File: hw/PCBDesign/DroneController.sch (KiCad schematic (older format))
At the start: 5 parts, among them J1 SerialDebug

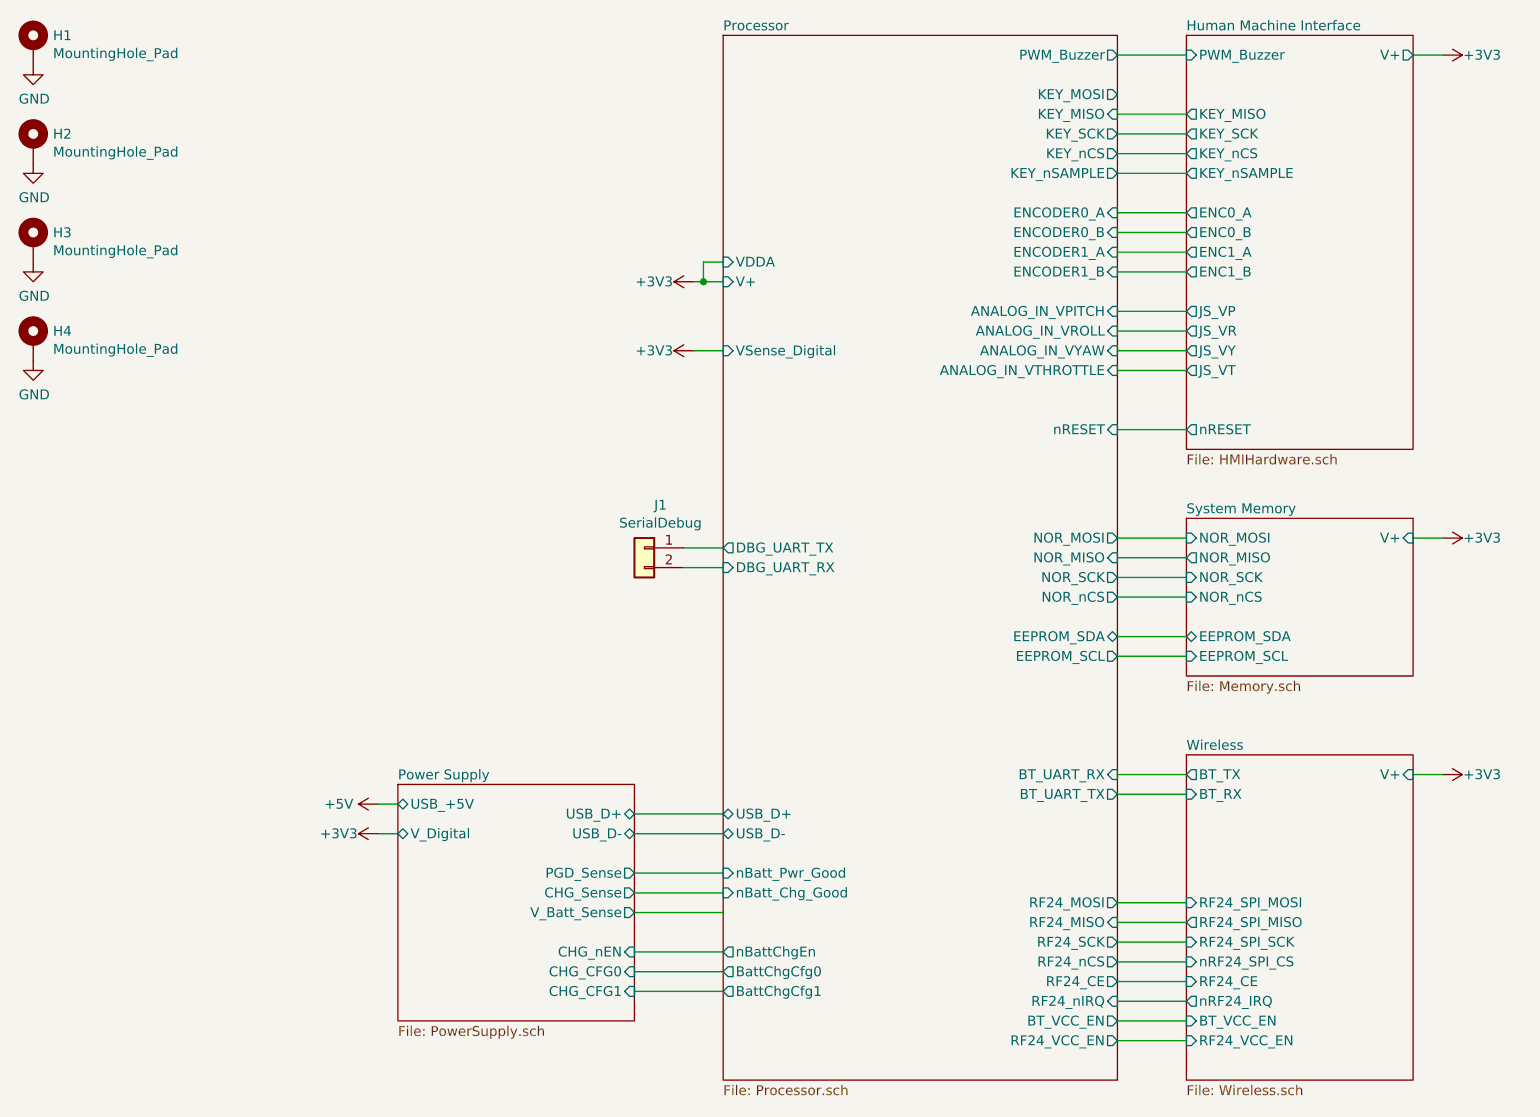
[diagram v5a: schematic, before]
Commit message: Routed most of the core peripherals
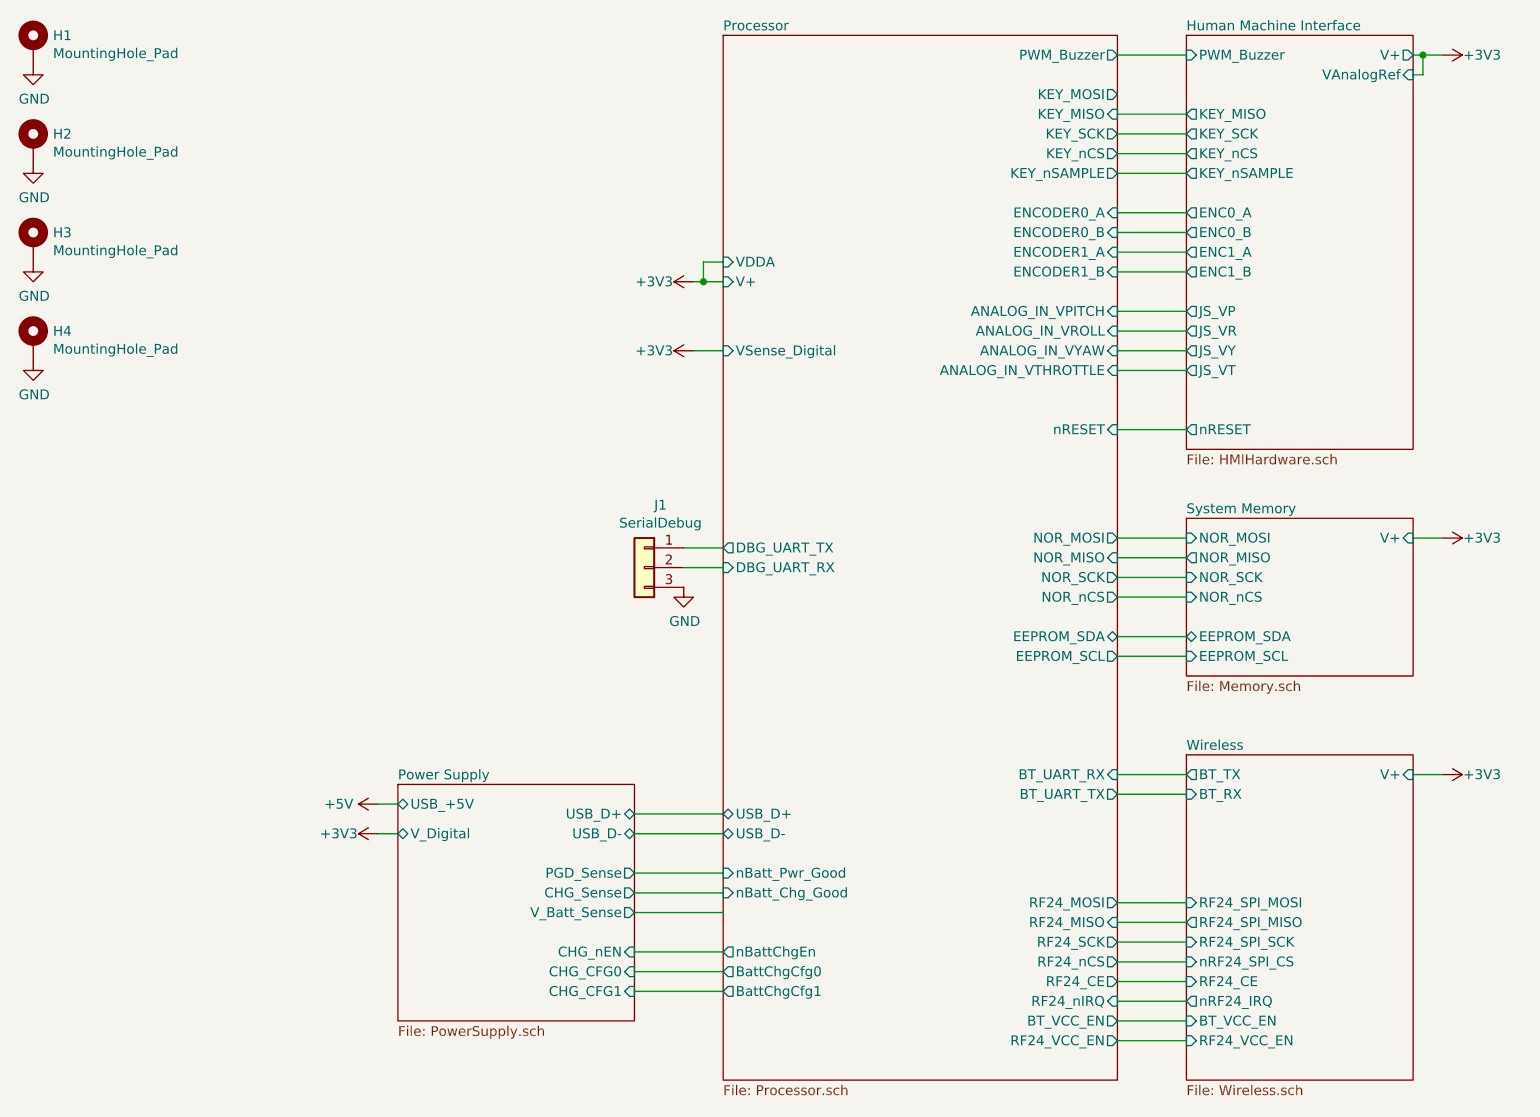
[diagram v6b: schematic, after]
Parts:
- removed J1: SerialDebug, Connector_PinHeader_2.54mm:PinHeader_1x02_P2.54mm_Vertical, symbol Connector_Generic:Conn_01x02
- added J1: SerialDebug, Connector_PinHeader_2.54mm:PinHeader_1x03_P2.54mm_Vertical, symbol Connector_Generic:Conn_01x03
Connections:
- net GND: now also J1.3 (Pin_3)
- net Processor/DBG_UART_RX: now also J1.2 (Pin_2)
- net Processor/DBG_UART_TX: now also J1.1 (Pin_1)
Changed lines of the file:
@@
 F15 "V+" O R 8000 1100 50
 F16 "nRESET" O L 6850 3000 50
+F17 "VAnalogRef" I R 8000 1200 50
 $EndSheet
 $Sheet
@@
 F0 "Wireless" 50
 F1 "Wireless.sch" 50
-F5 "BT_RX" I L 6850 4850 50
-F6 "BT_TX" O L 6850 4750 50
-F7 "RF24_SPI_MOSI" I L 6850 5400 50
-F8 "RF24_SPI_MISO" O L 6850 5500 50
-F9 "RF24_SPI_SCK" I L 6850 5600 50
-F10 "nRF24_SPI_CS" I L 6850 5700 50
-F11 "RF24_CE" I L 6850 5800 50
-F12 "nRF24_IRQ" O L 6850 5900 50
-F13 "V+" I R 8000 4750 50
-F14 "BT_VCC_EN" I L 6850 6000 50
-F15 "RF24_VCC_EN" I L 6850 6100 50
+F2 "BT_RX" I L 6850 4850 50
+F3 "BT_TX" O L 6850 4750 50
+F4 "RF24_SPI_MOSI" I L 6850 5400 50
+F5 "RF24_SPI_MISO" O L 6850 5500 50
+F6 "RF24_SPI_SCK" I L 6850 5600 50
+F7 "nRF24_SPI_CS" I L 6850 5700 50
+F8 "RF24_CE" I L 6850 5800 50
+F9 "nRF24_IRQ" O L 6850 5900 50
+F10 "V+" I R 8000 4750 50
+F11 "BT_VCC_EN" I L 6850 6000 50
+F12 "RF24_VCC_EN" I L 6850 6100 50
 $EndSheet
 $Comp
@@
 F1 "PowerSupply.sch" 50
 F2 "V_Digital" B L 2850 5050 50
-F5 "USB_D+" B R 4050 4950 50
-F6 "USB_D-" B R 4050 5050 50
-F7 "USB_+5V" B L 2850 4900 50
-F8 "PGD_Sense" O R 4050 5250 50
-F9 "CHG_Sense" O R 4050 5350 50
-F10 "CHG_nEN" I R 4050 5650 50
-F11 "CHG_CFG0" I R 4050 5750 50
-F12 "CHG_CFG1" I R 4050 5850 50
-F13 "V_Batt_Sense" O R 4050 5450 50
+F3 "USB_D+" B R 4050 4950 50
+F4 "USB_D-" B R 4050 5050 50
+F5 "USB_+5V" B L 2850 4900 50
+F6 "PGD_Sense" O R 4050 5250 50
+F7 "CHG_Sense" O R 4050 5350 50
+F8 "CHG_nEN" I R 4050 5650 50
+F9 "CHG_CFG0" I R 4050 5750 50
+F10 "CHG_CFG1" I R 4050 5850 50
+F11 "V_Batt_Sense" O R 4050 5450 50
 $EndSheet
 $Sheet
@@
 F4 "nBatt_Pwr_Good" I L 4500 5250 50
 F5 "nBatt_Chg_Good" I L 4500 5350 50
-F7 "nBattChgEn" O L 4500 5650 50
-F8 "BattChgCfg0" O L 4500 5750 50
-F9 "BattChgCfg1" O L 4500 5850 50
-F10 "BT_UART_RX" I R 6500 4750 50
-F11 "BT_UART_TX" O R 6500 4850 50
-F15 "RF24_MOSI" O R 6500 5400 50
-F16 "RF24_MISO" I R 6500 5500 50
-F17 "RF24_SCK" O R 6500 5600 50
-F18 "RF24_nCS" O R 6500 5700 50
-F19 "RF24_CE" O R 6500 5800 50
-F20 "RF24_nIRQ" I R 6500 5900 50
-F21 "NOR_MOSI" O R 6500 3550 50
-F22 "NOR_MISO" I R 6500 3650 50
-F23 "NOR_SCK" O R 6500 3750 50
-F24 "NOR_nCS" O R 6500 3850 50
-F25 "EEPROM_SDA" B R 6500 4050 50
-F26 "EEPROM_SCL" O R 6500 4150 50
-F27 "VSense_Digital" I L 4500 2600 50
-F30 "V+" I L 4500 2250 50
-F31 "nRESET" I R 6500 3000 50
-F32 "PWM_Buzzer" O R 6500 1100 50
-F33 "KEY_MOSI" O R 6500 1300 50
-F34 "KEY_MISO" I R 6500 1400 50
-F35 "KEY_SCK" O R 6500 1500 50
-F36 "KEY_nCS" O R 6500 1600 50
-F37 "KEY_nSAMPLE" O R 6500 1700 50
-F38 "ENCODER0_A" I R 6500 1900 50
-F39 "ENCODER0_B" I R 6500 2000 50
-F40 "ENCODER1_A" I R 6500 2100 50
-F41 "ENCODER1_B" I R 6500 2200 50
-F42 "ANALOG_IN_VPITCH" I R 6500 2400 50
-F43 "ANALOG_IN_VROLL" I R 6500 2500 50
-F44 "ANALOG_IN_VYAW" I R 6500 2600 50
-F45 "ANALOG_IN_VTHROTTLE" I R 6500 2700 50
-F46 "VDDA" I L 4500 2150 50
-F47 "DBG_UART_TX" O L 4500 3600 50
-F48 "DBG_UART_RX" I L 4500 3700 50
-F49 "BT_VCC_EN" O R 6500 6000 50
-F50 "RF24_VCC_EN" O R 6500 6100 50
+F6 "nBattChgEn" O L 4500 5650 50
+F7 "BattChgCfg0" O L 4500 5750 50
+F8 "BattChgCfg1" O L 4500 5850 50
+F9 "BT_UART_RX" I R 6500 4750 50
+F10 "BT_UART_TX" O R 6500 4850 50
+F11 "RF24_MOSI" O R 6500 5400 50
+F12 "RF24_MISO" I R 6500 5500 50
+F13 "RF24_SCK" O R 6500 5600 50
+F14 "RF24_nCS" O R 6500 5700 50
+F15 "RF24_CE" O R 6500 5800 50
+F16 "RF24_nIRQ" I R 6500 5900 50
+F17 "NOR_MOSI" O R 6500 3550 50
+F18 "NOR_MISO" I R 6500 3650 50
+F19 "NOR_SCK" O R 6500 3750 50
+F20 "NOR_nCS" O R 6500 3850 50
+F21 "EEPROM_SDA" B R 6500 4050 50
+F22 "EEPROM_SCL" O R 6500 4150 50
+F23 "VSense_Digital" I L 4500 2600 50
+F24 "V+" I L 4500 2250 50
+F25 "nRESET" I R 6500 3000 50
+F26 "PWM_Buzzer" O R 6500 1100 50
+F27 "KEY_MOSI" O R 6500 1300 50
+F28 "KEY_MISO" I R 6500 1400 50
+F29 "KEY_SCK" O R 6500 1500 50
+F30 "KEY_nCS" O R 6500 1600 50
+F31 "KEY_nSAMPLE" O R 6500 1700 50
+F32 "ENCODER0_A" I R 6500 1900 50
+F33 "ENCODER0_B" I R 6500 2000 50
+F34 "ENCODER1_A" I R 6500 2100 50
+F35 "ENCODER1_B" I R 6500 2200 50
+F36 "ANALOG_IN_VPITCH" I R 6500 2400 50
+F37 "ANALOG_IN_VROLL" I R 6500 2500 50
+F38 "ANALOG_IN_VYAW" I R 6500 2600 50
+F39 "ANALOG_IN_VTHROTTLE" I R 6500 2700 50
+F40 "VDDA" I L 4500 2150 50
+F41 "DBG_UART_TX" O L 4500 3600 50
+F42 "DBG_UART_RX" I L 4500 3700 50
+F43 "BT_VCC_EN" O R 6500 6000 50
+F44 "RF24_VCC_EN" O R 6500 6100 50
 $EndSheet
 Wire Wire Line
@@
 $EndComp
 Wire Wire Line
-	8150 1100 8000 1100
+	8150 1100 8050 1100
 Wire Wire Line
 	6500 3000 6850 3000
@@
 Wire Wire Line
 	6500 6100 6850 6100
-$Comp
-L Connector_Generic:Conn_01x02 J1
-U 1 1 604BEF1D
-P 4100 3600
-F 0 "J1" H 4018 3817 50  0000 C CNN
-F 1 "SerialDebug" H 4018 3726 50  0000 C CNN
-F 2 "Connector_PinHeader_2.54mm:PinHeader_1x02_P2.54mm_Vertical" H 4100 3600 50  0001 C CNN
-F 3 "~" H 4100 3600 50  0001 C CNN
-	1    4100 3600
-	-1   0    0    -1
-$EndComp
 Wire Wire Line
 	4300 3600 4500 3600
@@
 Wire Wire Line
 	4400 2250 4500 2250
+$Comp
+L Connector_Generic:Conn_01x03 J1
+U 1 1 6059D97C
+P 4100 3700
+F 0 "J1" H 4018 4017 50  0000 C CNN
+F 1 "SerialDebug" H 4018 3926 50  0000 C CNN
+F 2 "Connector_PinHeader_2.54mm:PinHeader_1x03_P2.54mm_Vertical" H 4100 3700 50  0001 C CNN
+F 3 "~" H 4100 3700 50  0001 C CNN
+	1    4100 3700
+	-1   0    0    -1
+$EndComp
+$Comp
+L power:GND #PWR08
+U 1 1 6059E0DC
+P 4300 3800
+F 0 "#PWR08" H 4300 3550 50  0001 C CNN
+F 1 "GND" H 4305 3627 50  0000 C CNN
+F 2 "" H 4300 3800 50  0001 C CNN
+F 3 "" H 4300 3800 50  0001 C CNN
+	1    4300 3800
+	1    0    0    -1
+$EndComp
+Wire Wire Line
+	8000 1200 8050 1200
+Wire Wire Line
+	8050 1200 8050 1100
+Connection ~ 8050 1100
+Wire Wire Line
+	8050 1100 8000 1100
 $EndSCHEMATC

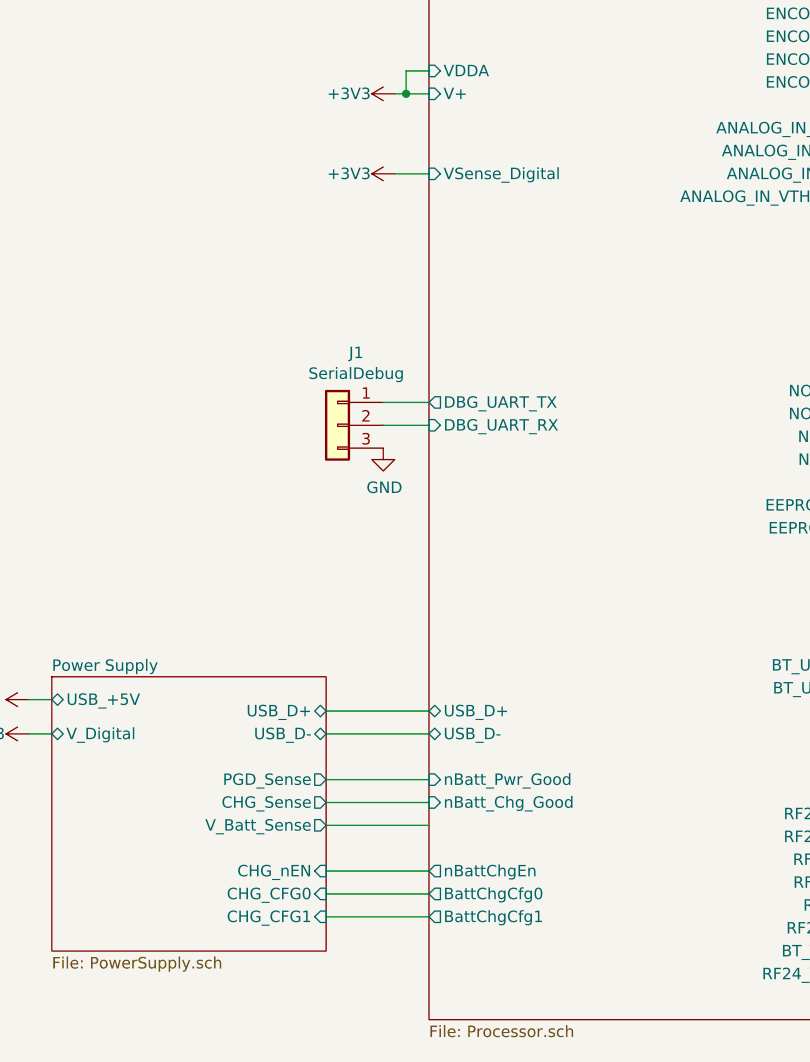
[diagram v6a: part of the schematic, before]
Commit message: Adjust components for lowest build cost
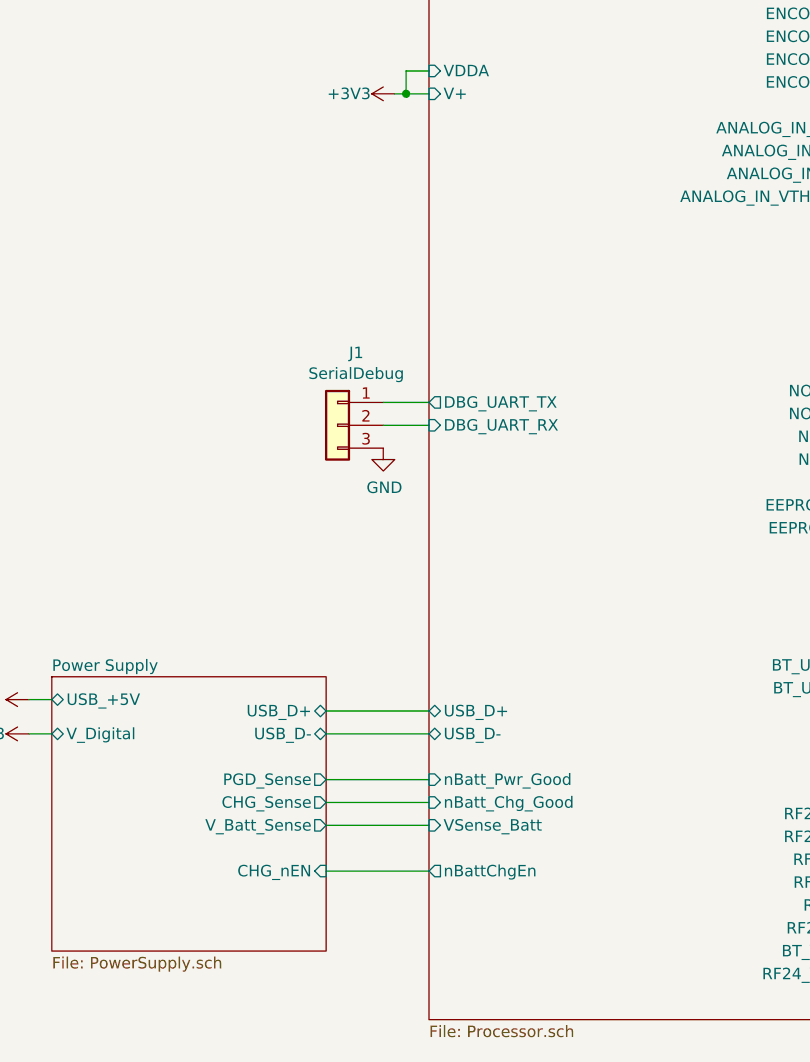
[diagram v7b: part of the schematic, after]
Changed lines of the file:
@@
 F7 "CHG_Sense" O R 4050 5350 50
 F8 "CHG_nEN" I R 4050 5650 50
-F9 "CHG_CFG0" I R 4050 5750 50
-F10 "CHG_CFG1" I R 4050 5850 50
 F11 "V_Batt_Sense" O R 4050 5450 50
 $EndSheet
@@
 F5 "nBatt_Chg_Good" I L 4500 5350 50
 F6 "nBattChgEn" O L 4500 5650 50
-F7 "BattChgCfg0" O L 4500 5750 50
-F8 "BattChgCfg1" O L 4500 5850 50
-F9 "BT_UART_RX" I R 6500 4750 50
-F10 "BT_UART_TX" O R 6500 4850 50
-F11 "RF24_MOSI" O R 6500 5400 50
-F12 "RF24_MISO" I R 6500 5500 50
-F13 "RF24_SCK" O R 6500 5600 50
-F14 "RF24_nCS" O R 6500 5700 50
-F15 "RF24_CE" O R 6500 5800 50
-F16 "RF24_nIRQ" I R 6500 5900 50
-F17 "NOR_MOSI" O R 6500 3550 50
-F18 "NOR_MISO" I R 6500 3650 50
-F19 "NOR_SCK" O R 6500 3750 50
-F20 "NOR_nCS" O R 6500 3850 50
-F21 "EEPROM_SDA" B R 6500 4050 50
-F22 "EEPROM_SCL" O R 6500 4150 50
-F23 "VSense_Digital" I L 4500 2600 50
-F24 "V+" I L 4500 2250 50
-F25 "nRESET" I R 6500 3000 50
-F26 "PWM_Buzzer" O R 6500 1100 50
-F27 "KEY_MOSI" O R 6500 1300 50
-F28 "KEY_MISO" I R 6500 1400 50
-F29 "KEY_SCK" O R 6500 1500 50
-F30 "KEY_nCS" O R 6500 1600 50
-F31 "KEY_nSAMPLE" O R 6500 1700 50
-F32 "ENCODER0_A" I R 6500 1900 50
-F33 "ENCODER0_B" I R 6500 2000 50
-F34 "ENCODER1_A" I R 6500 2100 50
-F35 "ENCODER1_B" I R 6500 2200 50
-F36 "ANALOG_IN_VPITCH" I R 6500 2400 50
-F37 "ANALOG_IN_VROLL" I R 6500 2500 50
-F38 "ANALOG_IN_VYAW" I R 6500 2600 50
-F39 "ANALOG_IN_VTHROTTLE" I R 6500 2700 50
-F40 "VDDA" I L 4500 2150 50
-F41 "DBG_UART_TX" O L 4500 3600 50
-F42 "DBG_UART_RX" I L 4500 3700 50
-F43 "BT_VCC_EN" O R 6500 6000 50
-F44 "RF24_VCC_EN" O R 6500 6100 50
+F7 "BT_UART_RX" I R 6500 4750 50
+F8 "BT_UART_TX" O R 6500 4850 50
+F9 "RF24_MOSI" O R 6500 5400 50
+F10 "RF24_MISO" I R 6500 5500 50
+F11 "RF24_SCK" O R 6500 5600 50
+F12 "RF24_nCS" O R 6500 5700 50
+F13 "RF24_CE" O R 6500 5800 50
+F14 "RF24_nIRQ" I R 6500 5900 50
+F15 "NOR_MOSI" O R 6500 3550 50
+F16 "NOR_MISO" I R 6500 3650 50
+F17 "NOR_SCK" O R 6500 3750 50
+F18 "NOR_nCS" O R 6500 3850 50
+F19 "EEPROM_SDA" B R 6500 4050 50
+F20 "EEPROM_SCL" O R 6500 4150 50
+F21 "V+" I L 4500 2250 50
+F22 "nRESET" I R 6500 3000 50
+F23 "PWM_Buzzer" O R 6500 1100 50
+F24 "KEY_MOSI" O R 6500 1300 50
+F25 "KEY_MISO" I R 6500 1400 50
+F26 "KEY_SCK" O R 6500 1500 50
+F27 "KEY_nCS" O R 6500 1600 50
+F28 "KEY_nSAMPLE" O R 6500 1700 50
+F29 "ENCODER0_A" I R 6500 1900 50
+F30 "ENCODER0_B" I R 6500 2000 50
+F31 "ENCODER1_A" I R 6500 2100 50
+F32 "ENCODER1_B" I R 6500 2200 50
+F33 "ANALOG_IN_VPITCH" I R 6500 2400 50
+F34 "ANALOG_IN_VROLL" I R 6500 2500 50
+F35 "ANALOG_IN_VYAW" I R 6500 2600 50
+F36 "ANALOG_IN_VTHROTTLE" I R 6500 2700 50
+F37 "VDDA" I L 4500 2150 50
+F38 "DBG_UART_TX" O L 4500 3600 50
+F39 "DBG_UART_RX" I L 4500 3700 50
+F40 "BT_VCC_EN" O R 6500 6000 50
+F41 "RF24_VCC_EN" O R 6500 6100 50
+F42 "VSense_Batt" I L 4500 5450 50
 $EndSheet
 Wire Wire Line
@@
 Wire Wire Line
 	4050 5650 4500 5650
-Wire Wire Line
-	4050 5750 4500 5750
-Wire Wire Line
-	4050 5850 4500 5850
 $Comp
 L power:+3V3 #PWR011
@@
 	6500 4150 6850 4150
 $Comp
-L power:+3V3 #PWR07
-U 1 1 6064DFA8
-P 4350 2600
-F 0 "#PWR07" H 4350 2450 50  0001 C CNN
-F 1 "+3V3" V 4350 2800 50  0000 C CNN
-F 2 "" H 4350 2600 50  0001 C CNN
-F 3 "" H 4350 2600 50  0001 C CNN
-	1    4350 2600
-	0    -1   -1   0
-$EndComp
-Wire Wire Line
-	4350 2600 4500 2600
-$Comp
 L power:+3V3 #PWR06
